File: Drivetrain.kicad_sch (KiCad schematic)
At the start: 0 parts

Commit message: Drivetrain: STM32 core, dual CAN, LEDs, self-test, test points, footprints
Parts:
- added C35, C36, C37, C38, C40, C42, C43, C45, C46, C47, C48, C49, C50, C55: 100nF, Capacitor_SMD:C_0603_1608Metric, symbol Device:C
- added C39, C41: 4.7uF, Capacitor_SMD:C_0805_2012Metric, symbol Device:C
- added C44: 1uF, Capacitor_SMD:C_0603_1608Metric, symbol Device:C
- added C51, C52, C53, C54: 22pF, Capacitor_SMD:C_0603_1608Metric, symbol Device:C
- added D10, D7, D8, D9: LED, LED_THT:LED_D3.0mm, symbol Device:LED
- added D6: LED, Resistor_SMD:R_0603_1608Metric, symbol Device:LED
- added FB1: 600R@100MHz, Inductor_SMD:L_0603_1608Metric, symbol Device:FerriteBead_Small
- added J5: SWD, Connector_PinHeader_2.54mm:PinHeader_1x06_P2.54mm_Vertical, symbol Connector_Generic:Conn_01x06
- added J6: CAN_A_PROBE, Connector_PinHeader_2.54mm:PinHeader_1x02_P2.54mm_Vertical, symbol Connector_Generic:Conn_01x02
- added J7: CAN_B_PROBE, Connector_PinHeader_2.54mm:PinHeader_1x02_P2.54mm_Vertical, symbol Connector_Generic:Conn_01x02
- added J8: Conn_01x13, Connector_PinHeader_2.54mm:PinHeader_1x13_P2.54mm_Vertical, symbol Connector_Generic:Conn_01x13
- added J9: Conn_01x03, Connector_PinHeader_2.54mm:PinHeader_1x03_P2.54mm_Vertical, symbol Connector_Generic:Conn_01x03
- added R26, R27, R28, R29, R30, R33: 10k, Resistor_SMD:R_0603_1608Metric, symbol Device:R
- added R31, R32: 120R, Resistor_SMD:R_0603_1608Metric, symbol Device:R
- added R34, R35, R36, R37, R38: 220, Resistor_SMD:R_0603_1608Metric, symbol Device:R
- added SW5, SW6: 219-2MSTR, Button_Switch_SMD:SW_DIP_SPSTx02_Slide_6.7x6.64mm_W8.61mm_P2.54mm_LowProfile, symbol Switch:SW_DIP_x02
- added SW7, SW8: CVS-01TB, Button_Switch_SMD:SW_DIP_SPSTx01_Slide_Copal_CVS-01xB_W5.9mm_P1mm, symbol Switch:SW_DIP_x01
- added SW9: SW_Push, Button_Switch_THT:SW_PUSH_6mm, symbol Switch:SW_Push
- added TP18: DT_ERR, TestPoint:TestPoint_Keystone_5015_Micro_Mini, symbol Connector:TestPoint
- added TP19: DT_SELF_TEST, TestPoint:TestPoint_Keystone_5015_Micro_Mini, symbol Connector:TestPoint
- added U10, U9: MCP2515T-I/ST, Package_SO:TSSOP-20_4.4x6.5mm_P0.65mm, symbol Interface_CAN_LIN:MCP2515-xST
- added U11, U12: SN65HVD230, Package_SO:SOIC-8_3.9x4.9mm_P1.27mm, symbol Interface_CAN_LIN:SN65HVD230
- added U8: STM32F401RETx, Package_QFP:LQFP-64_10x10mm_P0.5mm, symbol MCU_ST_STM32F4:STM32F401RETx
- added Y3, Y4: 16 MHz, Crystal:Crystal_SMD_3225-4Pin_3.2x2.5mm, symbol Device:Crystal_GND24
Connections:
- new net: R30.2, U12.8 (Rs)
- new net: U10.1 (TXCAN), U12.1 (D)
- new net: C48.1, R28.1, U10.19 (~{RESET})
- new net: U10.2 (RXCAN), U12.4 (R)
- new net: SW6.1, U12.7 (CANH)
- new net: SW6.2, U12.6 (CANL)
- new net: D9.2 (A), R37.2
- new net: D10.2 (A), R38.2
- new net: C47.1, R27.1, U9.19 (~{RESET})
- new net: D8.2 (A), R36.2
- new net: U11.1 (D), U9.1 (TXCAN)
- new net: U11.4 (R), U9.2 (RXCAN)
- new net: C43.2, C44.2, FB1.2, U8.13 (VREF+)
- new net: SW5.2, U11.6 (CANL)
- new net: SW5.1, U11.7 (CANH)
- new net: R29.2, U11.8 (Rs)
- new net: C41.2, U8.30 (VCAP1)
- new net: D6.2 (A), R34.2
- new net: D7.2 (A), R35.2
- new net: R31.1, SW7.1
- new net: R26.1, U8.60 (BOOT0)
- new net: R32.1, SW8.1
- new net 3V3: C35.2, C36.2, C37.1, C38.1, C39.1, C40.2, C45.1, C46.1, C49.1, C50.1, FB1.1, J5.1 (Pin_1), R27.2, R28.2, R33.1, U10.20 (VDD), U11.3 (VCC), U12.3 (VCC), U8.1 (VBAT), U8.19 (VDD), U8.32 (VDD), U8.48 (VDD), U8.64 (VDD), U9.20 (VDD)
- new net CANH_A: J6.1 (Pin_1), R31.2, SW5.4
- new net CANH_B: J7.1 (Pin_1), R32.2, SW6.4
- new net CANL_A: J6.2 (Pin_2), SW5.3, SW7.2
- new net CANL_B: J7.2 (Pin_2), SW6.3, SW8.2
- new net DT_CAN_A_CS: U8.58 (PB6), U9.18 (~{CS})
- new net DT_CAN_A_INT: U8.43 (PA10), U9.13 (~{INT})
- new net DT_CAN_B_CS: U10.18 (~{CS}), U8.38 (PC7)
- new net DT_CAN_B_INT: U10.13 (~{INT}), U8.57 (PB5)
- new net DT_DEG_A: J8.7 (Pin_7), R35.1, U8.9 (PC1)
- new net DT_DEG_B: J8.8 (Pin_8), R34.1, U8.8 (PC0)
- new net DT_ERR: R38.1, TP18.1, U8.53 (PC12)
- new net DT_RL: J8.12 (Pin_12), R36.1, U8.33 (PB12)
- new net DT_RR: J8.13 (Pin_13), R37.1, U8.34 (PB13)
- new net DT_SELF_TEST: C55.1, R33.2, SW9.2, TP19.1, U8.2 (PC13)
- new net DT_SPI_MISO: U10.17 (SO), U8.22 (PA6), U9.17 (SO)
- new net DT_SPI_MOSI: U10.16 (SI), U8.23 (PA7), U9.16 (SI)
- new net DT_SPI_SCLK: U10.14 (SCK), U8.21 (PA5), U9.14 (SCK)
- new net DT_TP_CAN_RX_A: J8.3 (Pin_3), U8.10 (PC2)
- new net DT_TP_CAN_RX_B: J8.4 (Pin_4), U8.11 (PC3)
- new net DT_TP_CAN_TX_A: J8.5 (Pin_5), U8.51 (PC10)
- new net DT_TP_CAN_TX_B: J8.6 (Pin_6), U8.52 (PC11)
- new net DT_UART_RX: J9.1 (Pin_1), U8.17 (PA3)
- new net DT_UART_TX: J9.2 (Pin_2), U8.16 (PA2)
- new net GND: C35.1, C36.1, C37.2, C38.2, C39.2, C40.1, C41.1, C42.1, C43.1, C44.1, C45.2, C46.2, C47.2, C48.2, C49.2, C50.2, C51.2, C52.2, C53.2, C54.2, C55.2, D10.1 (K), D6.1 (K), D7.1 (K), D8.1 (K), D9.1 (K), J5.3 (Pin_3), J8.1 (Pin_1), J8.2 (Pin_2), J9.3 (Pin_3), R26.2, R29.1, R30.1, SW9.1, U10.10 (VSS), U11.2 (GND), U12.2 (GND), U8.12 (VSSA), U8.18 (VSS), U8.31 (VSS), U8.47 (VSS), U8.63 (VSS), U9.10 (VSS), Y3.2 (G), Y3.4 (G), Y4.2 (G), Y4.4 (G)
- new net NRST: C42.2, J5.5 (Pin_5), U8.7 (NRST)
- new net OSC_DT_A1: C51.1, U9.9 (OSC1), Y3.1
- new net OSC_DT_A2: C53.1, U9.8 (OSC2), Y3.3
- new net OSC_DT_B1: C52.1, U10.8 (OSC2), Y4.1
- new net OSC_DT_B2: C54.1, U10.9 (OSC1), Y4.3
- new net SWCLK: J5.2 (Pin_2), U8.49 (PA14)
- new net SWDIO: J5.4 (Pin_4), U8.46 (PA13)
- new net SWO: J5.6 (Pin_6), U8.55 (PB3)
- no-connect marks 0 -> 16
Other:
- note added: "CAN A Interface"
- note added: "CAN B Interface"
- note added: "Connectors & Test Points"
- note added: "Only one probe header per CAN bus is needed."
- note added: "STM Breakout"

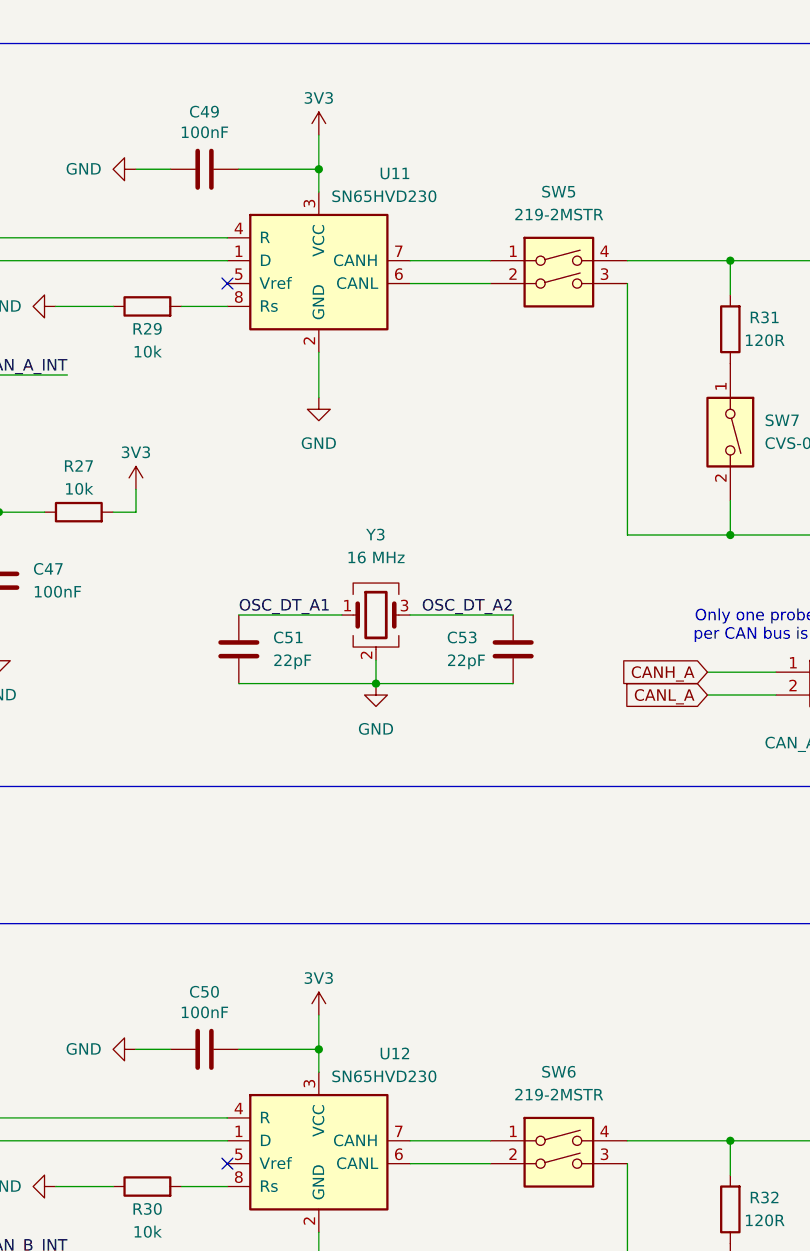
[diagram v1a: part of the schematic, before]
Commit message: changed MPN on CAN
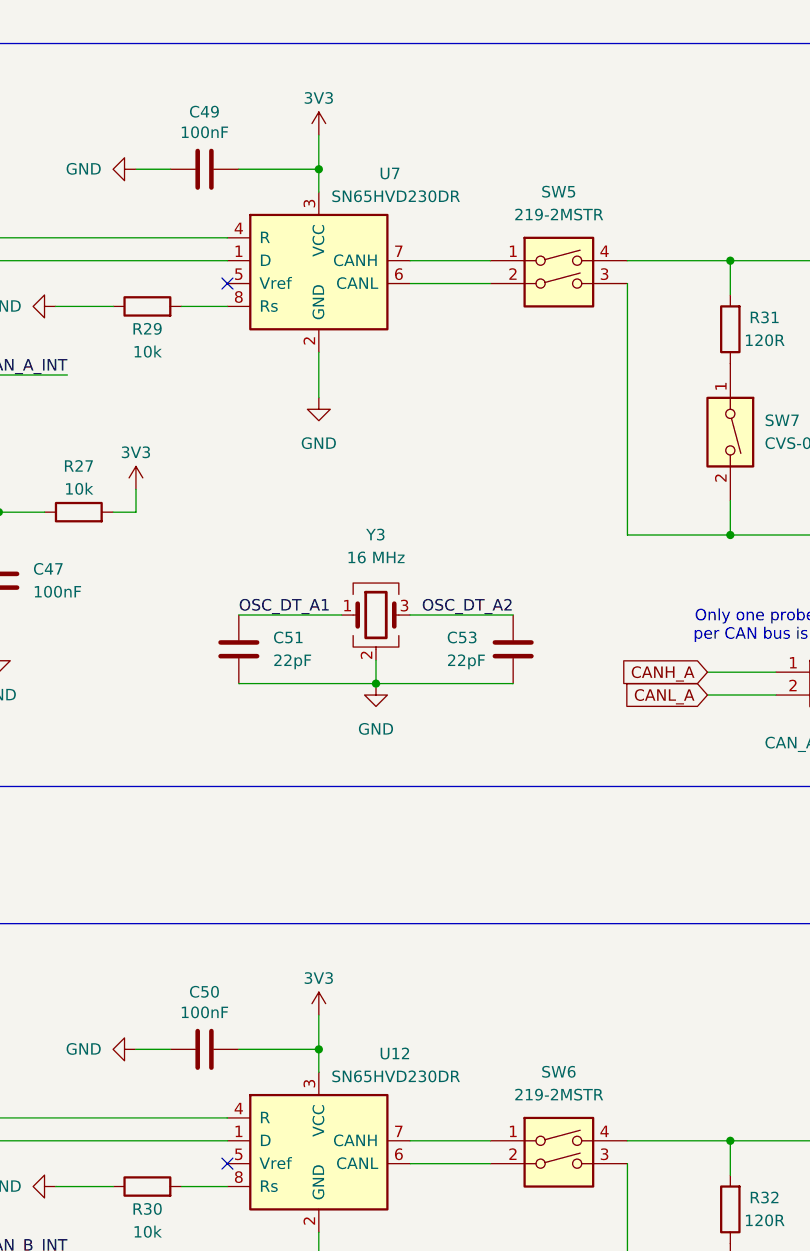
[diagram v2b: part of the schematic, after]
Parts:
- removed U11: SN65HVD230, Package_SO:SOIC-8_3.9x4.9mm_P1.27mm, symbol Interface_CAN_LIN:SN65HVD230
- added U7: SN65HVD230DR, Package_SO:SOIC-8_3.9x4.9mm_P1.27mm, symbol Interface_CAN_LIN:SN65HVD230
- U12: value SN65HVD230 -> SN65HVD230DR; Assembly (none) -> SMT; JLCPCB Category (none) -> Extended; LCSC Part # (none) -> C12084; Manufacturer (none) -> Texas Instruments; Manufacturer Part Number (none) -> SN65HVD230DR; Source (none) -> JLCPCB
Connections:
- net 3V3: now also U7.3 (VCC)
- net GND: now also U7.2 (GND)
- net at U9.1 (TXCAN): now also U7.1 (D)
- net at U9.2 (RXCAN): now also U7.4 (R)
- net at SW5.2: now also U7.6 (CANL)
- net at SW5.1: now also U7.7 (CANH)
- net at R29.2: now also U7.8 (Rs)

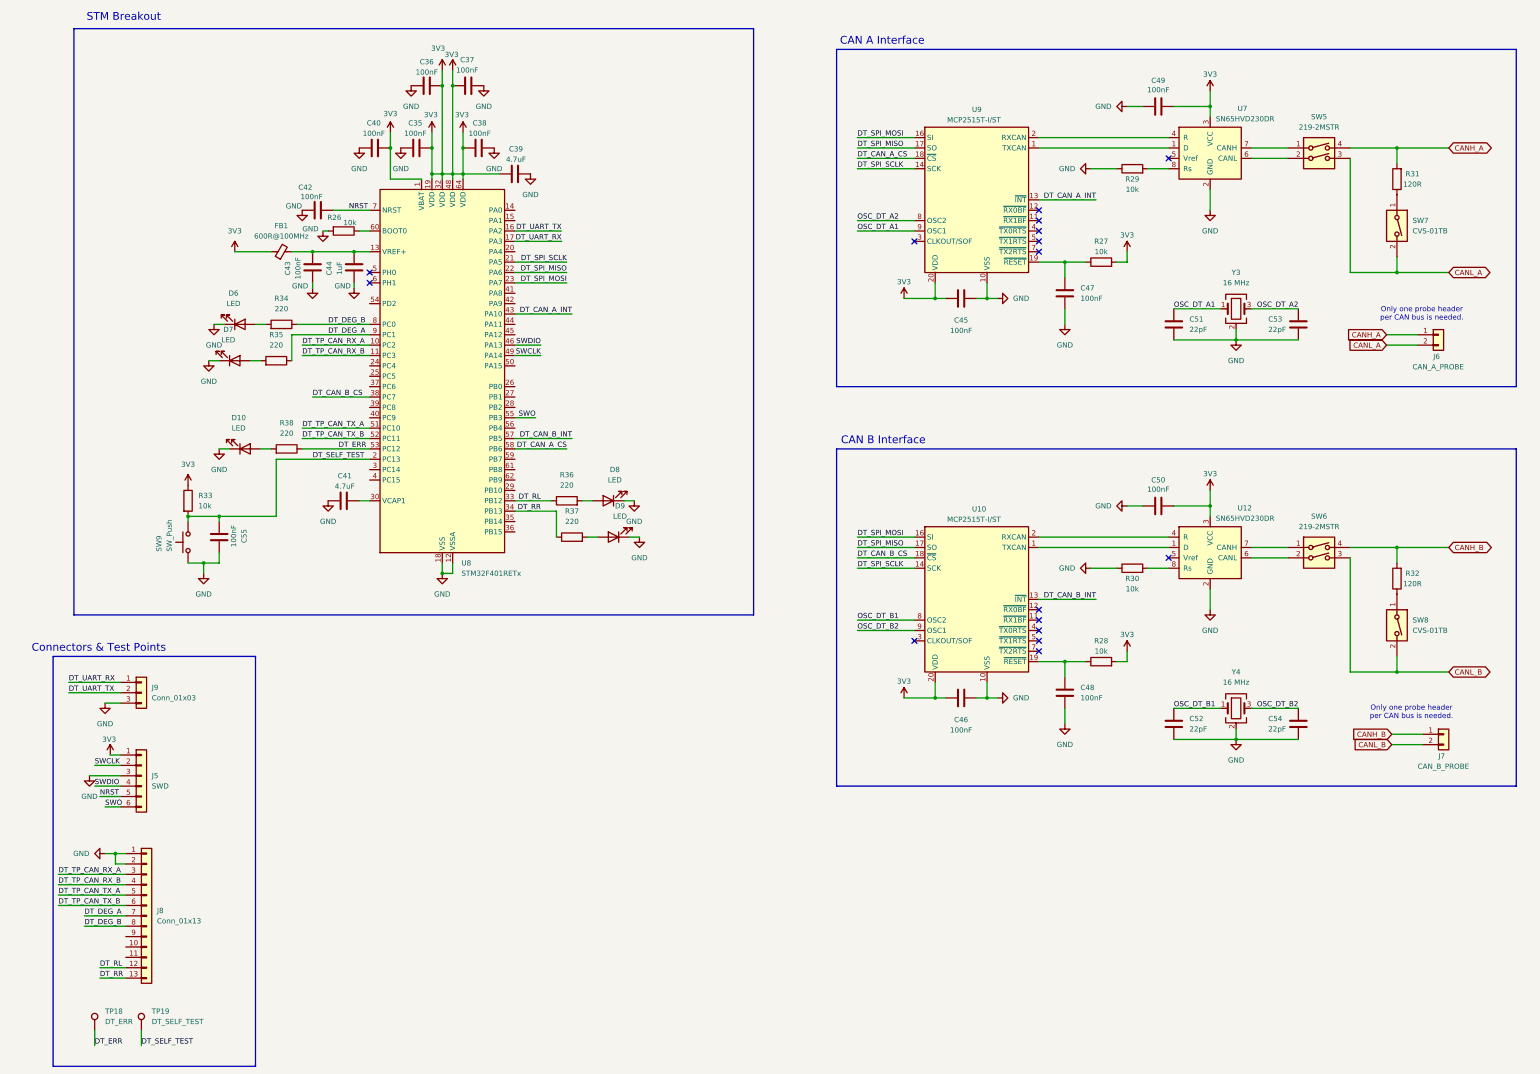
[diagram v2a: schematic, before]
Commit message: Re-annotate whole schematic (sheet x100); drivetrain SCLK fix, BOM fields, footprints
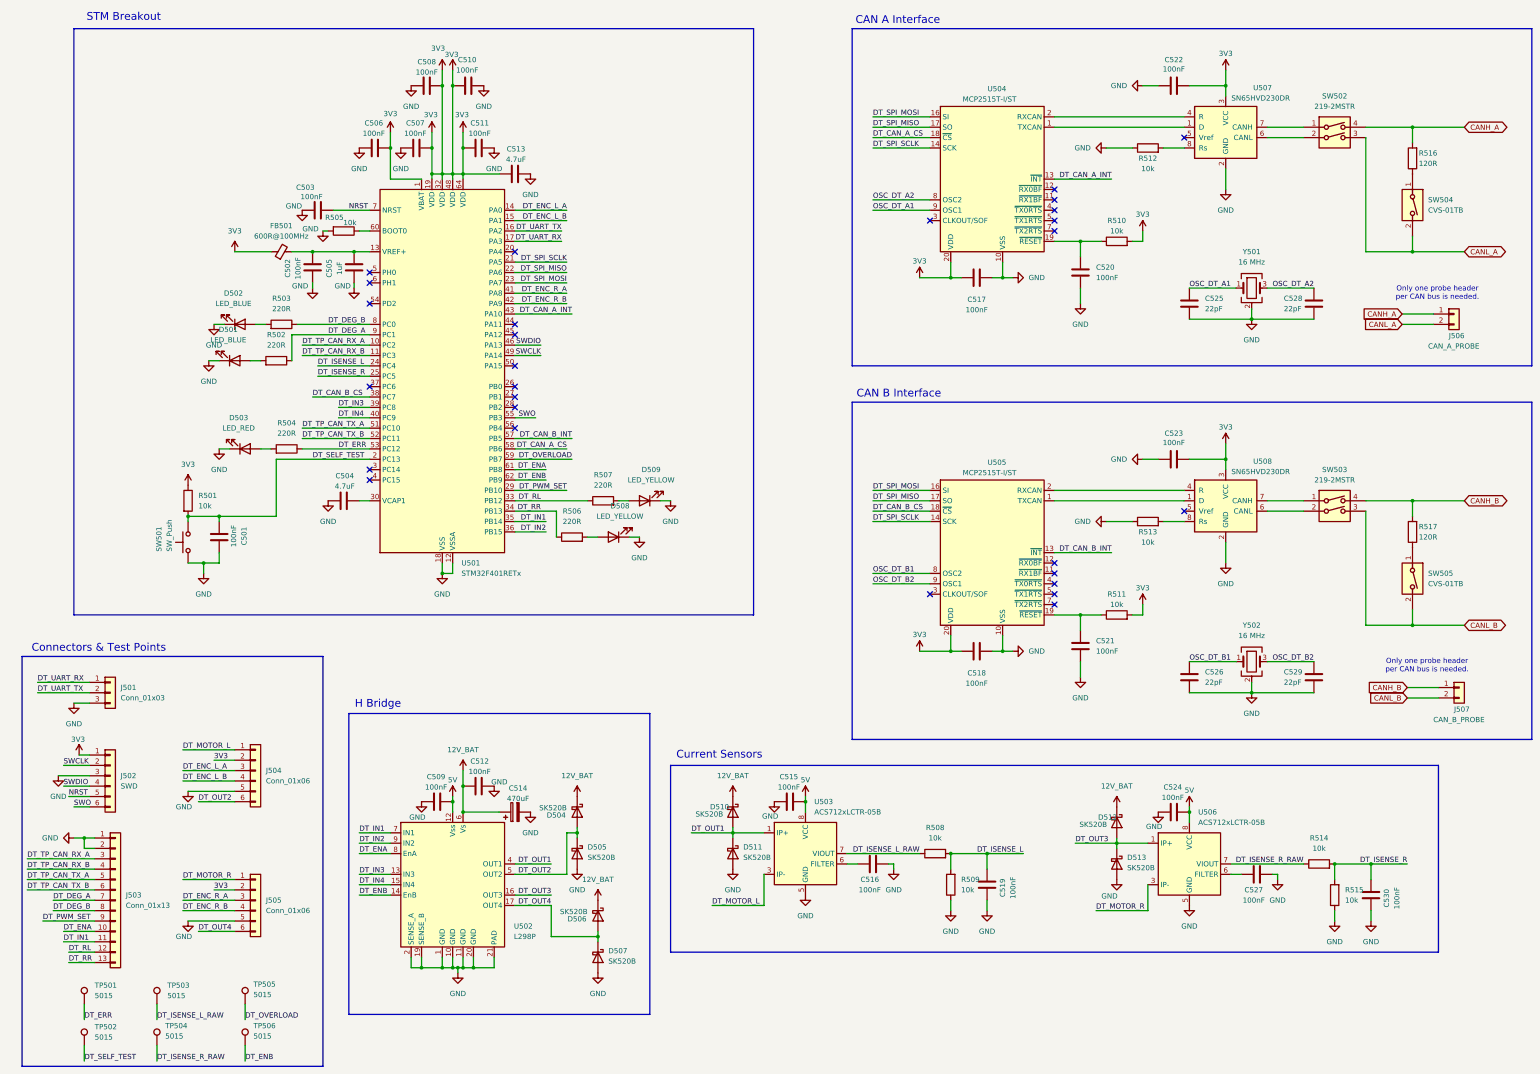
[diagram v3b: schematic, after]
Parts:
- removed C45, C46, C47, C48, C49, C50: 100nF, Capacitor_SMD:C_0603_1608Metric, symbol Device:C
- removed C51, C52, C53, C54: 22pF, Capacitor_SMD:C_0603_1608Metric, symbol Device:C
- removed J6: CAN_A_PROBE, Connector_PinHeader_2.54mm:PinHeader_1x02_P2.54mm_Vertical, symbol Connector_Generic:Conn_01x02
- removed J7: CAN_B_PROBE, Connector_PinHeader_2.54mm:PinHeader_1x02_P2.54mm_Vertical, symbol Connector_Generic:Conn_01x02
- removed R27, R28, R29, R30: 10k, Resistor_SMD:R_0603_1608Metric, symbol Device:R
- removed R31, R32: 120R, Resistor_SMD:R_0603_1608Metric, symbol Device:R
- removed SW5, SW6: 219-2MSTR, Button_Switch_SMD:SW_DIP_SPSTx02_Slide_6.7x6.64mm_W8.61mm_P2.54mm_LowProfile, symbol Switch:SW_DIP_x02
- removed SW7, SW8: CVS-01TB, Button_Switch_SMD:SW_DIP_SPSTx01_Slide_Copal_CVS-01xB_W5.9mm_P1mm, symbol Switch:SW_DIP_x01
- removed U10, U9: MCP2515T-I/ST, Package_SO:TSSOP-20_4.4x6.5mm_P0.65mm, symbol Interface_CAN_LIN:MCP2515-xST
- removed U12, U7: SN65HVD230DR, Package_SO:SOIC-8_3.9x4.9mm_P1.27mm, symbol Interface_CAN_LIN:SN65HVD230
- removed Y3, Y4: 16 MHz, Crystal:Crystal_SMD_3225-4Pin_3.2x2.5mm, symbol Device:Crystal_GND24
- added C509, C512, C515, C516, C517, C518, C519, C520, C521, C522, C523, C524, C527, C530: 100nF, Capacitor_SMD:C_0603_1608Metric, symbol Device:C
- added C514: 470uF, Capacitor_THT:CP_Radial_D8.0mm_P3.50mm, symbol Device:C_Polarized
- added C525, C526, C528, C529: 22pF, Capacitor_SMD:C_0603_1608Metric, symbol Device:C
- added D504, D505, D506, D507, D510, D511, D512, D513: SK520B, Diode_SMD:D_SMB, symbol Device:D_Schottky
- added J504, J505: Conn_01x06, Connector_JST:JST_PH_B6B-PH-SM4-TB_1x06-1MP_P2.00mm_Vertical, symbol Connector_Generic:Conn_01x06
- added J506: CAN_A_PROBE, Connector_PinHeader_2.54mm:PinHeader_1x02_P2.54mm_Vertical, symbol Connector_Generic:Conn_01x02
- added J507: CAN_B_PROBE, Connector_PinHeader_2.54mm:PinHeader_1x02_P2.54mm_Vertical, symbol Connector_Generic:Conn_01x02
- added R508, R509, R510, R511, R512, R513, R514, R515: 10k, Resistor_SMD:R_0603_1608Metric, symbol Device:R
- added R516, R517: 120R, Resistor_SMD:R_0603_1608Metric, symbol Device:R
- added SW502, SW503: 219-2MSTR, Button_Switch_SMD:SW_DIP_SPSTx02_Slide_6.7x6.64mm_W8.61mm_P2.54mm_LowProfile, symbol Switch:SW_DIP_x02
- added SW504, SW505: CVS-01TB, Button_Switch_SMD:SW_DIP_SPSTx01_Slide_Copal_CVS-01xB_W5.9mm_P1mm, symbol Switch:SW_DIP_x01
- added TP503, TP504, TP505, TP506: 5015, TestPoint:TestPoint_Keystone_5015_Micro_Mini, symbol Connector:TestPoint
- added U502: L298P, Package_SO:HSOP-20-1EP_11.0x15.9mm_P1.27mm_SlugDown, symbol Driver_Motor:L298P
- added U503, U506: ACS712xLCTR-05B, Package_SO:SOIC-8_3.9x4.9mm_P1.27mm, symbol Sensor_Current:ACS712xLCTR-05B
- added U504, U505: MCP2515T-I/ST, Package_SO:TSSOP-20_4.4x6.5mm_P0.65mm, symbol Interface_CAN_LIN:MCP2515-xST
- added U507, U508: SN65HVD230DR, Package_SO:SOIC-8_3.9x4.9mm_P1.27mm, symbol Interface_CAN_LIN:SN65HVD230
- added Y501, Y502: 16 MHz, Crystal:Crystal_SMD_3225-4Pin_3.2x2.5mm, symbol Device:Crystal_GND24
- C501: renamed from C55; Assembly (none) -> Hand-solder; JLCPCB Category (none) -> Extended; LCSC Part # (none) -> C172738; Manufacturer (none) -> KEMET; Manufacturer Part Number (none) -> C0603C104K3RACAUTO; Source (none) -> DigiKey
- C502: renamed from C43; Assembly (none) -> Hand-solder; JLCPCB Category (none) -> Extended; LCSC Part # (none) -> C172738; Manufacturer (none) -> KEMET; Manufacturer Part Number (none) -> C0603C104K3RACAUTO; Source (none) -> DigiKey
- C503: renamed from C42; Assembly (none) -> Hand-solder; JLCPCB Category (none) -> Extended; LCSC Part # (none) -> C172738; Manufacturer (none) -> KEMET; Manufacturer Part Number (none) -> C0603C104K3RACAUTO; Source (none) -> DigiKey
- C504: renamed from C41; Assembly (none) -> Hand-solder; Manufacturer (none) -> Murata; Manufacturer Part Number (none) -> GRM219R61E475KA73D; Source (none) -> Lab stock
- C505: renamed from C44; Assembly (none) -> Hand-solder; JLCPCB Category (none) -> Basic; LCSC Part # (none) -> C15849; Manufacturer (none) -> Samsung Electro-Mechanics; Manufacturer Part Number (none) -> CL10A105KB8NNNC; Source (none) -> DigiKey
- C506: renamed from C40; Assembly (none) -> Hand-solder; JLCPCB Category (none) -> Extended; LCSC Part # (none) -> C172738; Manufacturer (none) -> KEMET; Manufacturer Part Number (none) -> C0603C104K3RACAUTO; Source (none) -> DigiKey
- C507: renamed from C35; Assembly (none) -> Hand-solder; JLCPCB Category (none) -> Extended; LCSC Part # (none) -> C172738; Manufacturer (none) -> KEMET; Manufacturer Part Number (none) -> C0603C104K3RACAUTO; Source (none) -> DigiKey
- C508: renamed from C36; Assembly (none) -> Hand-solder; JLCPCB Category (none) -> Extended; LCSC Part # (none) -> C172738; Manufacturer (none) -> KEMET; Manufacturer Part Number (none) -> C0603C104K3RACAUTO; Source (none) -> DigiKey
- C510: renamed from C37; Assembly (none) -> Hand-solder; JLCPCB Category (none) -> Extended; LCSC Part # (none) -> C172738; Manufacturer (none) -> KEMET; Manufacturer Part Number (none) -> C0603C104K3RACAUTO; Source (none) -> DigiKey
- C511: renamed from C38; Assembly (none) -> Hand-solder; JLCPCB Category (none) -> Extended; LCSC Part # (none) -> C172738; Manufacturer (none) -> KEMET; Manufacturer Part Number (none) -> C0603C104K3RACAUTO; Source (none) -> DigiKey
- C513: renamed from C39; Assembly (none) -> Hand-solder; Manufacturer (none) -> Murata; Manufacturer Part Number (none) -> GRM219R61E475KA73D; Source (none) -> Lab stock
- D501: renamed from D7; value LED -> LED_BLUE; Assembly (none) -> Hand-solder; Manufacturer (none) -> Würth Elektronik; Manufacturer Part Number (none) -> 151033BS03000; Source (none) -> DigiKey
- D502: renamed from D6; value LED -> LED_BLUE; footprint Resistor_SMD:R_0603_1608Metric -> LED_THT:LED_D3.0mm; Assembly (none) -> Hand-solder; Manufacturer (none) -> Würth Elektronik; Manufacturer Part Number (none) -> 151033BS03000; Source (none) -> DigiKey
- D503: renamed from D10; value LED -> LED_RED; Assembly (none) -> Hand-solder; JLCPCB Category (none) -> Extended; LCSC Part # (none) -> C6067185; Manufacturer (none) -> Würth Elektronik; Manufacturer Part Number (none) -> 151031SS06000; Source (none) -> Lab stock
- D508: renamed from D9; value LED -> LED_YELLOW; Assembly (none) -> Hand-solder; Manufacturer (none) -> Würth Elektronik; Manufacturer Part Number (none) -> 151031YS06000; Source (none) -> Lab stock
- D509: renamed from D8; value LED -> LED_YELLOW; Assembly (none) -> Hand-solder; Manufacturer (none) -> Würth Elektronik; Manufacturer Part Number (none) -> 151031YS06000; Source (none) -> Lab stock
- FB501: renamed from FB1; Assembly (none) -> Hand-solder; LCSC Part # 742863160 -> (none); Manufacturer (none) -> Würth Elektronik; Manufacturer Part Number (none) -> 742863160; Source (none) -> Lab stock
- J501: renamed from J9; Assembly (none) -> Hand-solder; Manufacturer (none) -> Samtec; Manufacturer Part Number (none) -> TSW-103-07-G-S; Source (none) -> DigiKey
- J502: renamed from J5; Assembly (none) -> Hand-solder; Manufacturer (none) -> Samtec; Manufacturer Part Number (none) -> TSW-106-07-G-S; Source (none) -> DigiKey
- J503: renamed from J8; Assembly (none) -> Hand-solder; Manufacturer (none) -> Samtec; Manufacturer Part Number (none) -> TSW-113-07-G-S; Source (none) -> DigiKey
- R501: renamed from R33; Assembly (none) -> Hand-solder; JLCPCB Category (none) -> Extended; LCSC Part # (none) -> C844918; Manufacturer (none) -> Vishay Dale; Manufacturer Part Number (none) -> CRCW060310K0FKEA; Source (none) -> Lab stock
- R502: renamed from R35; value 220 -> 220R; Assembly (none) -> Hand-solder; JLCPCB Category (none) -> Extended; LCSC Part # (none) -> C844757; Manufacturer (none) -> Vishay Dale; Manufacturer Part Number (none) -> CRCW0603220RFKEA; Source (none) -> DigiKey
- R503: renamed from R34; value 220 -> 220R; Assembly (none) -> Hand-solder; JLCPCB Category (none) -> Extended; LCSC Part # (none) -> C844757; Manufacturer (none) -> Vishay Dale; Manufacturer Part Number (none) -> CRCW0603220RFKEA; Source (none) -> DigiKey
- R504: renamed from R38; value 220 -> 220R; Assembly (none) -> Hand-solder; JLCPCB Category (none) -> Extended; LCSC Part # (none) -> C844757; Manufacturer (none) -> Vishay Dale; Manufacturer Part Number (none) -> CRCW0603220RFKEA; Source (none) -> DigiKey
- R505: renamed from R26; Assembly (none) -> Hand-solder; JLCPCB Category (none) -> Extended; LCSC Part # (none) -> C844918; Manufacturer (none) -> Vishay Dale; Manufacturer Part Number (none) -> CRCW060310K0FKEA; Source (none) -> Lab stock
- R506: renamed from R37; value 220 -> 220R; Assembly (none) -> Hand-solder; JLCPCB Category (none) -> Extended; LCSC Part # (none) -> C844757; Manufacturer (none) -> Vishay Dale; Manufacturer Part Number (none) -> CRCW0603220RFKEA; Source (none) -> DigiKey
- R507: renamed from R36; value 220 -> 220R; Assembly (none) -> Hand-solder; JLCPCB Category (none) -> Extended; LCSC Part # (none) -> C844757; Manufacturer (none) -> Vishay Dale; Manufacturer Part Number (none) -> CRCW0603220RFKEA; Source (none) -> DigiKey
- SW501: renamed from SW9; Assembly (none) -> Hand-solder; JLCPCB Category (none) -> Extended; LCSC Part # (none) -> C93157; Manufacturer (none) -> Omron; Manufacturer Part Number (none) -> B3F-1000; Source (none) -> DigiKey
- TP501: renamed from TP18; value DT_ERR -> 5015; Assembly (none) -> Hand-solder; JLCPCB Category (none) -> Extended; LCSC Part # (none) -> C2906768; Manufacturer (none) -> Keystone; Manufacturer Part Number (none) -> 5015; Source (none) -> Lab stock
- TP502: renamed from TP19; value DT_SELF_TEST -> 5015; Assembly (none) -> Hand-solder; JLCPCB Category (none) -> Extended; LCSC Part # (none) -> C2906768; Manufacturer (none) -> Keystone; Manufacturer Part Number (none) -> 5015; Source (none) -> Lab stock
- U501: renamed from U8; Assembly (none) -> Hand-solder; JLCPCB Category (none) -> Extended; LCSC Part # (none) -> C116978; Manufacturer (none) -> STMicroelectronics; Manufacturer Part Number (none) -> STM32F401RET6; Source (none) -> Lab stock
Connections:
- net 3V3: now also C517.1, C518.1, C522.1, C523.1, J504.2 (Pin_2), J505.2 (Pin_2), R510.2, R511.2, U504.20 (VDD), U505.20 (VDD), U507.3 (VCC), U508.3 (VCC)
- net CANH_A: now also J506.1 (Pin_1), R516.2, SW502.4
- net CANH_B: now also J507.1 (Pin_1), R517.2, SW503.4
- net CANL_A: now also J506.2 (Pin_2), SW502.3, SW504.2
- net CANL_B: now also J507.2 (Pin_2), SW503.3, SW505.2
- net DT_CAN_A_CS: now also U504.18 (~{CS})
- net DT_CAN_A_INT: now also U504.13 (~{INT})
- net DT_CAN_B_CS: now also U505.18 (~{CS})
- net DT_CAN_B_INT: now also U505.13 (~{INT})
- net DT_SPI_MISO: now also U504.17 (SO), U505.17 (SO)
- net DT_SPI_MOSI: now also U504.16 (SI), U505.16 (SI)
- net DT_SPI_SCLK: now also U504.14 (SCK), U505.14 (SCK)
- net GND: now also C509.1, C512.2, C514.2, C515.1, C516.2, C517.2, C518.2, C519.1, C520.2, C521.2, C522.2, C523.2, C524.1, C525.2, C526.2, C527.2, C528.2, C529.2, C530.1, D505.2 (A), D507.2 (A), D511.2 (A), D513.2 (A), J504.5 (Pin_5), J505.5 (Pin_5), R509.1, R512.1, R513.1, R515.1, U502.1 (GND), U502.10 (GND), U502.11 (GND), U502.19 (SENSE_B), U502.2 (SENSE_A), U502.20 (GND), U502.21 (PAD), U503.5 (GND), U504.10 (VSS), U505.10 (VSS), U506.5 (GND), U507.2 (GND), U508.2 (GND), Y501.2 (G), Y501.4 (G), Y502.2 (G), Y502.4 (G)
- net OSC_DT_A1: now also C525.1, U504.9 (OSC1), Y501.1
- net OSC_DT_A2: now also C528.1, U504.8 (OSC2), Y501.3
- net OSC_DT_B1: now also C526.1, U505.8 (OSC2), Y502.1
- net OSC_DT_B2: now also C529.1, U505.9 (OSC1), Y502.3
- net DT_ENA: now reaches J503.10 (Pin_10)
- net DT_ENA: now also U501.61 (PB8), U502.8 (EnA)
- net DT_IN1: now reaches J503.11 (Pin_11)
- net DT_IN1: now also U501.35 (PB14), U502.7 (IN1)
- net DT_PWM_SET: now reaches J503.9 (Pin_9)
- net DT_PWM_SET: now also U501.29 (PB10)
- net DT_ENC_L_A: now reaches U501.14 (PA0)
- net DT_ENC_L_A: now also J504.3 (Pin_3)
- net DT_ENC_L_B: now reaches U501.15 (PA1)
- net DT_ENC_L_B: now also J504.4 (Pin_4)
- net DT_ISENSE_L: now reaches U501.24 (PC4)
- net DT_ISENSE_L: now also C519.2, R508.2, R509.2
- net DT_ISENSE_R: now reaches U501.25 (PC5)
- net DT_ISENSE_R: now also C530.2, R514.2, R515.2
- net DT_IN2: now reaches U501.36 (PB15)
- net DT_IN2: now also U502.9 (IN2)
- net DT_IN3: now reaches U501.39 (PC8)
- net DT_IN3: now also U502.13 (IN3)
- net DT_IN4: now reaches U501.40 (PC9)
- net DT_IN4: now also U502.15 (IN4)
- net DT_ENC_R_A: now reaches U501.41 (PA8)
- net DT_ENC_R_A: now also J505.3 (Pin_3)
- net DT_ENC_R_B: now reaches U501.42 (PA9)
- net DT_ENC_R_B: now also J505.4 (Pin_4)
- net DT_OVERLOAD: now reaches U501.59 (PB7)
- net DT_OVERLOAD: now also TP505.1
- net DT_ENB: now reaches U501.62 (PB9)
- net DT_ENB: now also TP506.1, U502.14 (EnB)
- new net: R517.1, SW505.1
- new net: R512.2, U507.8 (Rs)
- new net: SW503.1, U508.7 (CANH)
- new net: SW503.2, U508.6 (CANL)
- new net: C520.1, R510.1, U504.19 (~{RESET})
- new net: R513.2, U508.8 (Rs)
- new net: C521.1, R511.1, U505.19 (~{RESET})
- new net: U504.1 (TXCAN), U507.1 (D)
- new net: U504.2 (RXCAN), U507.4 (R)
- new net: R516.1, SW504.1
- new net: U505.1 (TXCAN), U508.1 (D)
- new net: U505.2 (RXCAN), U508.4 (R)
- new net: C516.1, U503.6 (FILTER)
- new net: C527.1, U506.6 (FILTER)
- new net: SW502.2, U507.6 (CANL)
- new net: SW502.1, U507.7 (CANH)
- new net 12V_BAT: C512.1, C514.1, D504.1 (K), D506.1 (K), D510.1 (K), D512.1 (K), U502.6 (Vs)
- new net 5V: C509.2, C515.2, C524.2, U502.12 (Vss), U503.8 (VCC), U506.8 (VCC)
- new net DT_ISENSE_L_RAW: R508.1, TP503.1, U503.7 (VIOUT)
- new net DT_ISENSE_R_RAW: R514.1, TP504.1, U506.7 (VIOUT)
- new net DT_MOTOR_L: J504.1 (Pin_1), U503.3 (IP-), U503.4 (IP-)
- new net DT_MOTOR_R: J505.1 (Pin_1), U506.3 (IP-), U506.4 (IP-)
- new net DT_OUT1: D510.2 (A), D511.1 (K), U502.4 (OUT1), U503.1 (IP+), U503.2 (IP+)
- new net DT_OUT2: D504.2 (A), D505.1 (K), J504.6 (Pin_6), U502.5 (OUT2)
- new net DT_OUT3: D512.2 (A), D513.1 (K), U502.16 (OUT3), U506.1 (IP+), U506.2 (IP+)
- new net DT_OUT4: D506.2 (A), D507.1 (K), J505.6 (Pin_6), U502.17 (OUT4)
- no-connect marks 16 -> 28
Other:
- note added: "Current Sensors"
- note added: "H Bridge"
- moved on the sheet: D509, J501, J502, J503, R507, TP501, TP502
